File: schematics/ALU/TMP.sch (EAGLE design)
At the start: 11 parts

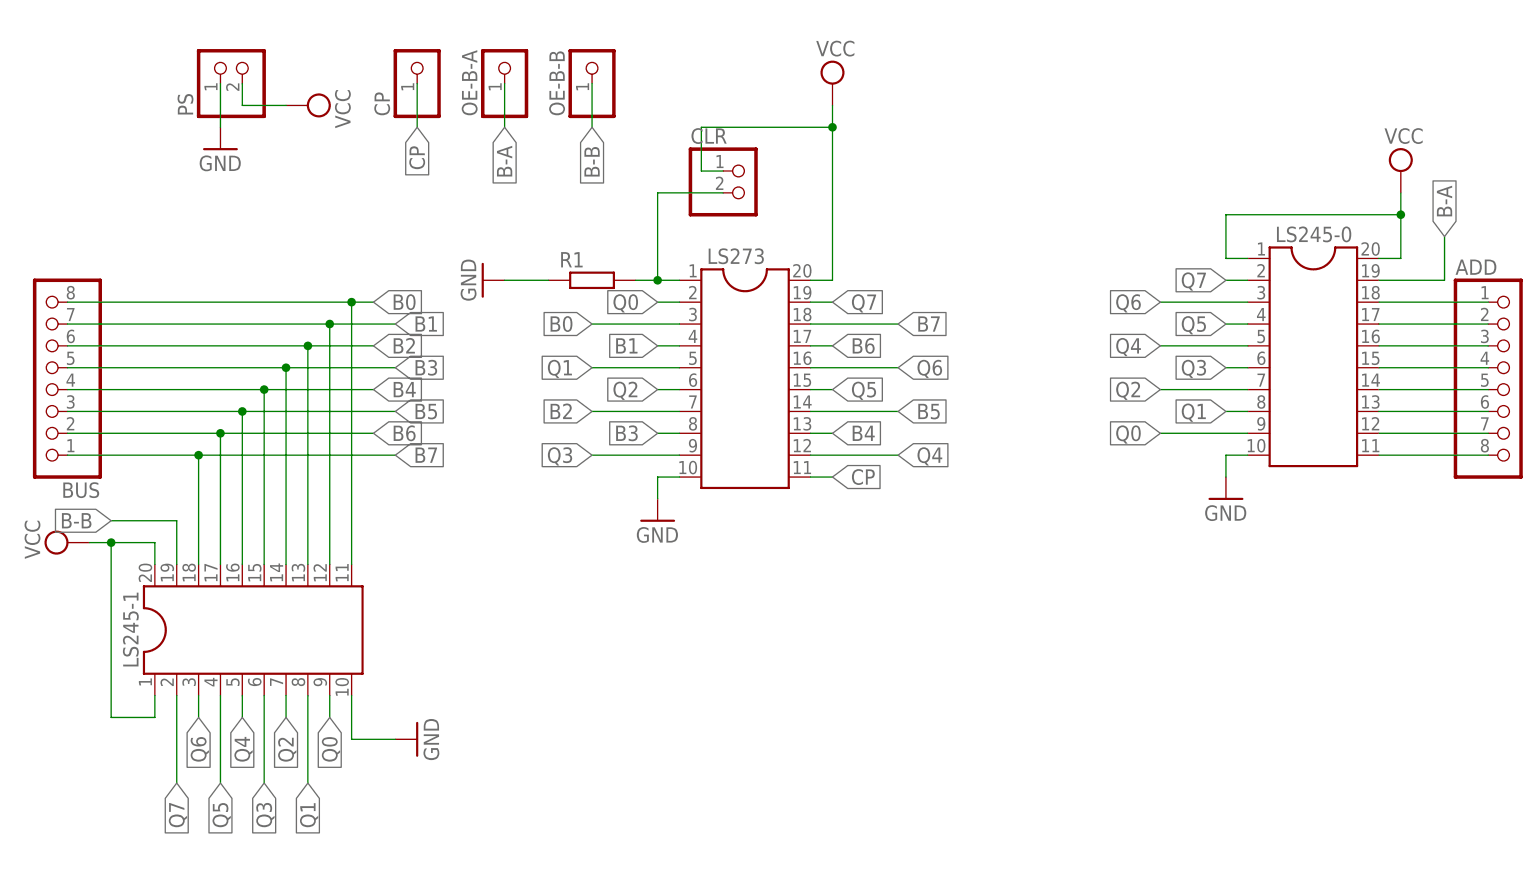
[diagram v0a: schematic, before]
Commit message: TMP (B) register doesnt need buffers.
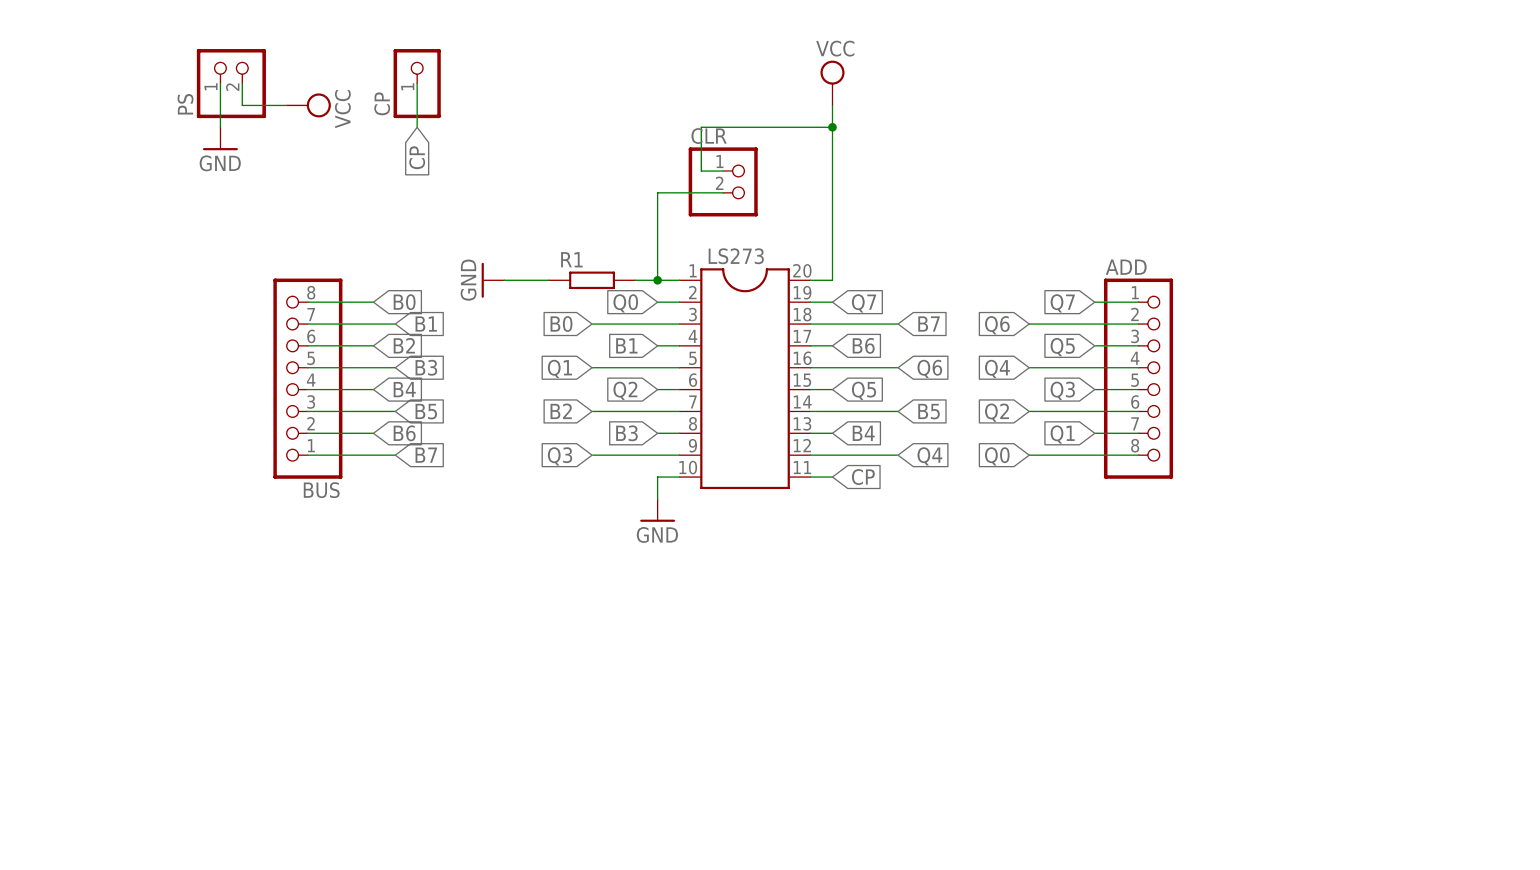
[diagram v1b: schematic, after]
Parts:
- removed LS245-0, LS245-1: (no value), ic-package:DIL20S
- removed OE-B-A, OE-B-B: (no value), pinhead:PINHD-1X1
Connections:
- removed net A0: ADD.1, LS245-0.18
- removed net A1: ADD.2, LS245-0.17
- removed net A2: ADD.3, LS245-0.16
- removed net A3: ADD.4, LS245-0.15
- removed net A4: ADD.5, LS245-0.14
- removed net A5: ADD.6, LS245-0.13
- removed net A6: ADD.7, LS245-0.12
- removed net A7: ADD.8, LS245-0.11
- removed net B-A: LS245-0.19, OE-B-A.1
- removed net B-B: LS245-1.19, OE-B-B.1
- net B0: no longer LS245-1.11
- net B1: no longer LS245-1.12
- net B2: no longer LS245-1.13
- net B3: no longer LS245-1.14
- net B4: no longer LS245-1.15
- net B5: no longer LS245-1.16
- net B6: no longer LS245-1.17
- net B7: no longer LS245-1.18
- net GND: no longer LS245-0.10, LS245-1.10
- net Q0: now also ADD.8; no longer LS245-0.9, LS245-1.9
- net Q1: now also ADD.7; no longer LS245-0.8, LS245-1.8
- net Q2: now also ADD.6; no longer LS245-0.7, LS245-1.7
- net Q3: now also ADD.5; no longer LS245-0.6, LS245-1.6
- net Q4: now also ADD.4; no longer LS245-0.5, LS245-1.5
- net Q5: now also ADD.3; no longer LS245-0.4, LS245-1.4
- net Q6: now also ADD.2; no longer LS245-0.3, LS245-1.3
- net Q7: now also ADD.1; no longer LS245-0.2, LS245-1.2
- net VCC: no longer LS245-0.1, LS245-0.20, LS245-1.1, LS245-1.20
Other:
- moved on the sheet: ADD, BUS
